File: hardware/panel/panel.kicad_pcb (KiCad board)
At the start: 2 copper layers, 62 x 101.5 mm, 1 part

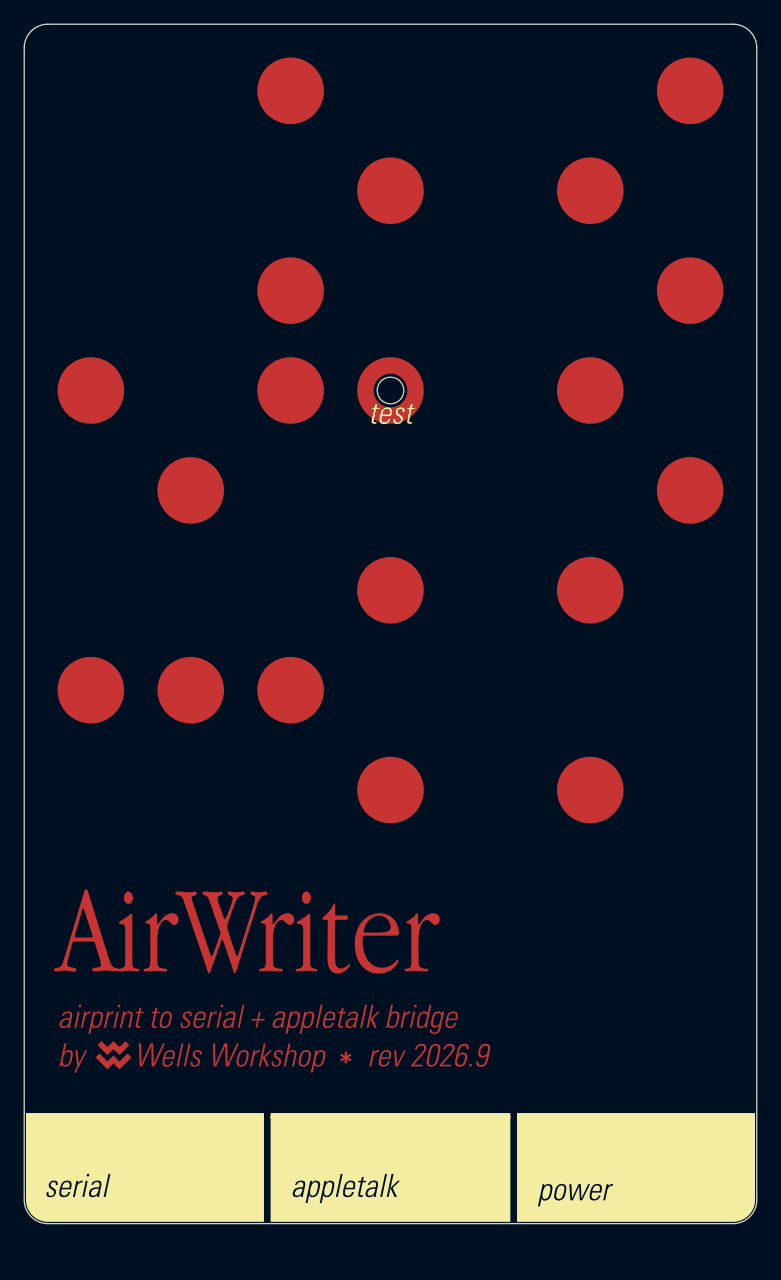
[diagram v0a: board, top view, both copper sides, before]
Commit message: Panel: fix mask-leaked plates, adopt taller re-export
svgelements yields the CONTENT of <mask> definitions as ordinary
elements during traversal - each label cell's mask rect (the full
cell bounds, inheriting fill="white" from the <mask> element) leaked
into silk.polys.json as a solid plate, which is why the label cells
rendered as flat panels instead of text-on-black.

svg2poly.py now strips <mask>...</mask> blocks from the raw SVG text
before parsing (their content must never become an element), and
separately parses each mask's own rect bbox from the raw text so any
element still carrying mask="url(#id)" gets clipped to it via
Sutherland-Hodgman rectangle clipping after flattening - the three
label cells' rule bars come out 0.225mm tall (clipped to the inside
half) instead of 0.45mm spilling above the cell. Raises a clear error
if a mask's content isn't reducible to a single axis-aligned rect.

Also adopts Wells's re-exported panel.svg ("Frame 9"): viewBox grew
0 0 1100 1801 -> 0 0 1100 1850 (62.0 x 104.27mm), grid unchanged (57
circles). Updates the panel-height and coordinate-bound test
constants to match; the SVG is the source of truth.

Verified: 9/9 tests green, kicad-cli DRC 0 violations, two
generate.sh runs produce a byte-identical panel.kicad_pcb, and the
re-rendered front face shows the label cells as white text + thin
rules on black (no plates), wordmark/subtitle and the test dot's
surviving annulus intact.

Refs: W-573
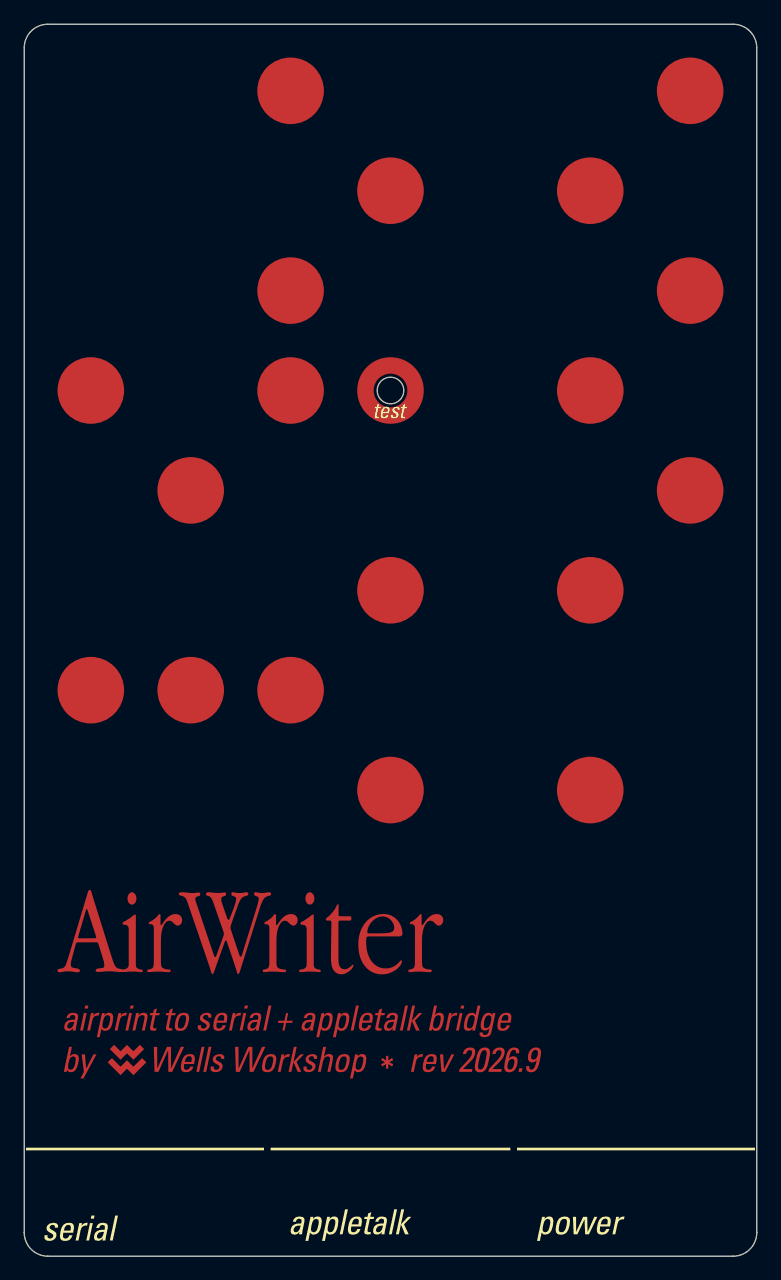
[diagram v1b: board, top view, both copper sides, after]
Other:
- board size 62 x 101.5 mm -> 62 x 104.3 mm
